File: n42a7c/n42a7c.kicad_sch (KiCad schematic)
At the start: 111 parts, among them J1 Conn_01x02_Pin, J2 Conn_01x02_Pin, SW1 CPG151101S11-16, SW10 CPG151101S11-16, SW11 CPG151101S11-16, SW12 CPG151101S11-16, SW13 CPG151101S11-16, SW14 CPG151101S11-16, SW15 CPG151101S11-16, SW16 CPG151101S11-16, SW17 CPG151101S11-16, SW18 CPG151101S11-16, SW19 CPG151101S11-16, SW2 CPG151101S11-16, SW20 CPG151101S11-16, SW21 CPG151101S11-16, SW22 CPG151101S11-16, SW23 CPG151101S11-16, SW24 CPG151101S11-16, SW25 CPG151101S11-16, SW26 CPG151101S11-16, SW27 CPG151101S11-16, SW28 CPG151101S11-16, SW29 CPG151101S11-16, SW3 CPG151101S11-16, SW30 CPG151101S11-16, SW31 CPG151101S11-16, SW32 CPG151101S11-16, SW33 CPG151101S11-16, SW34 CPG151101S11-16, SW35 CPG151101S11-16, SW36 CPG151101S11-16, SW37 CPG151101S11-16, SW38 CPG151101S11-16, SW39 CPG151101S11-16, SW4 CPG151101S11-16, SW40 CPG151101S11-16, SW41 CPG151101S11-16, SW42 CPG151101S11-16, SW5 CPG151101S11-16, SW6 CPG151101S11-16, SW7 CPG151101S11-16, SW8 CPG151101S11-16, SW9 CPG151101S11-16, U1 XIAO-nRF52840-SMD

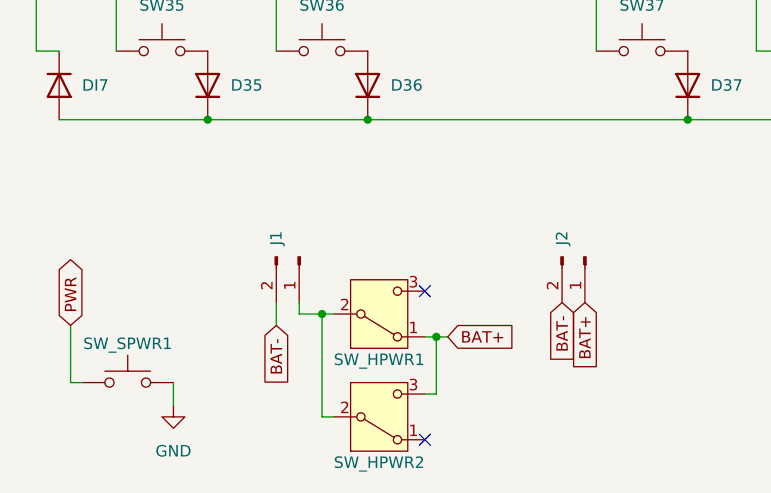
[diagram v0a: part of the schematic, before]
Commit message: revise SSAJ1x0100 footprint / symbol
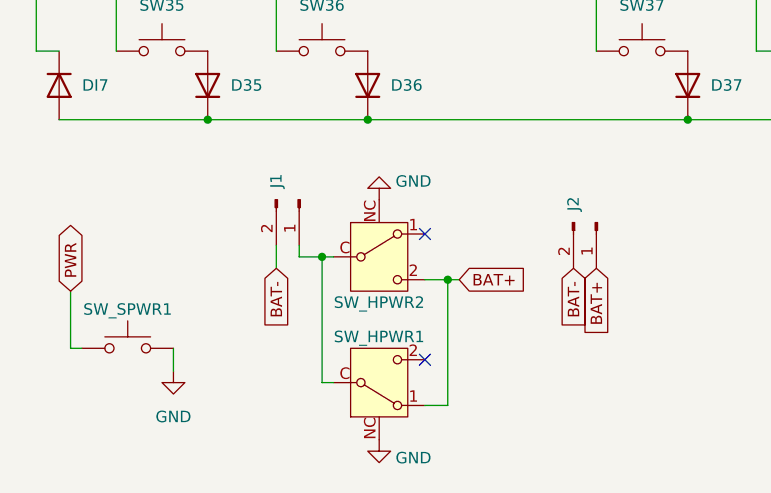
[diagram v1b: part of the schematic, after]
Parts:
- removed SW_HPWR1, SW_HPWR2: SSAJ120100, cscslib:SSAJ120100, symbol Switch:SW_SPDT
- added SW_HPWR1, SW_HPWR2: SSAJ110100, cscslib:SSAJ110100, symbol cscslib:SSAJ1x0100
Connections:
- net BAT+: now also SW_HPWR1.1 (A), SW_HPWR2.2 (C)
- net GND: now also SW_HPWR1.NC, SW_HPWR2.NC
- net at J1.1 (Pin_1): now also SW_HPWR1.C (B), SW_HPWR2.C (B)
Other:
- moved on the sheet: J1, J2, SW_SPWR1

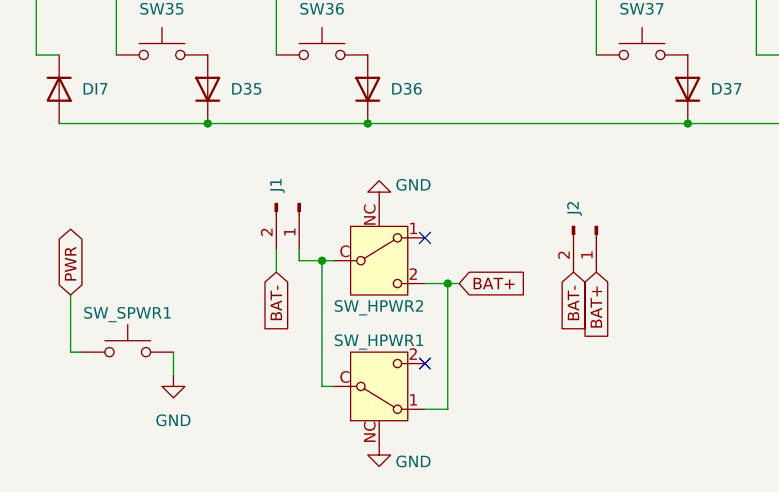
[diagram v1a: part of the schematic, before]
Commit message: revise power connector
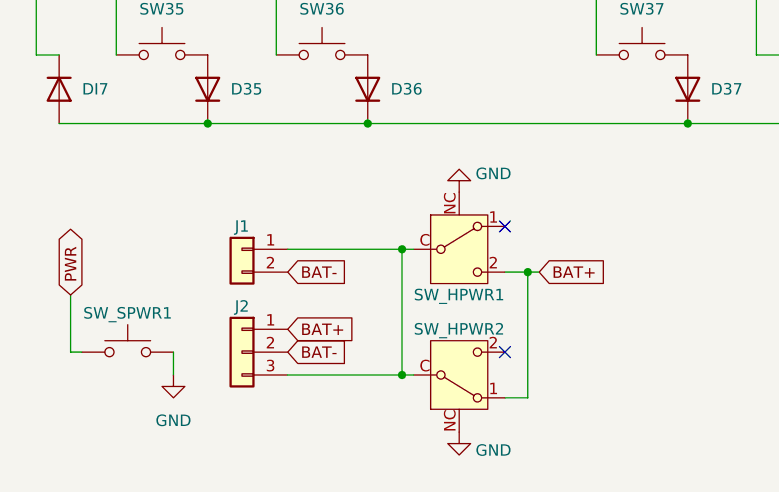
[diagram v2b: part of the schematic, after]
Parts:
- removed J1: Conn_01x02_Pin, Connector_JST:JST_PH_S2B-PH-K_1x02_P2.00mm_Horizontal, symbol Connector:Conn_01x02_Pin
- removed J2: Conn_01x02_Pin, Connector_PinHeader_2.54mm:PinHeader_1x02_P2.54mm_Vertical, symbol Connector:Conn_01x02_Pin
- added J1: Conn_01x02, Connector_JST:JST_PH_S2B-PH-K_1x02_P2.00mm_Horizontal, symbol Connector_Generic:Conn_01x02
- added J2: Conn_01x03, Connector_PinHeader_2.00mm:PinHeader_1x03_P2.00mm_Vertical, symbol Connector_Generic:Conn_01x03
- renumbered SW_HPWR2 to SW_HPWR1, SW_HPWR1 to SW_HPWR2
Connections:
- net BAT+: now also J2.1 (Pin_1)
- net BAT-: now also J1.2 (Pin_2), J2.2 (Pin_2)
- net GND: now also SW_SPWR1.1; no longer SW_SPWR1.2
- net PWR: now also SW_SPWR1.2; no longer SW_SPWR1.1
- net at SW_HPWR1.C (B), SW_HPWR2.C (B): now also J1.1 (Pin_1), J2.3 (Pin_3)
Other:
- moved on the sheet: SW_HPWR1, SW_HPWR2

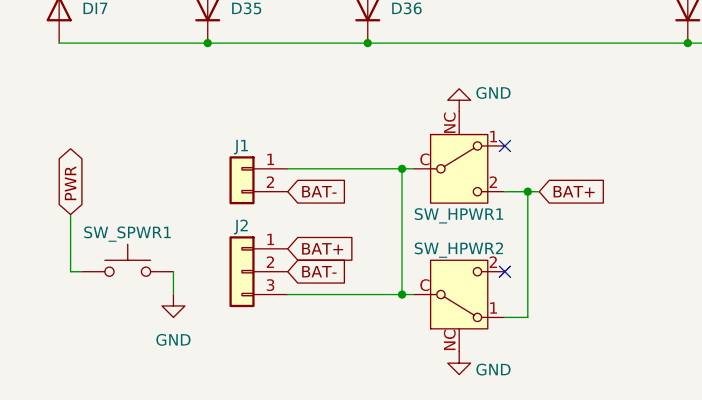
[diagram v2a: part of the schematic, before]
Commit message: revise power SW
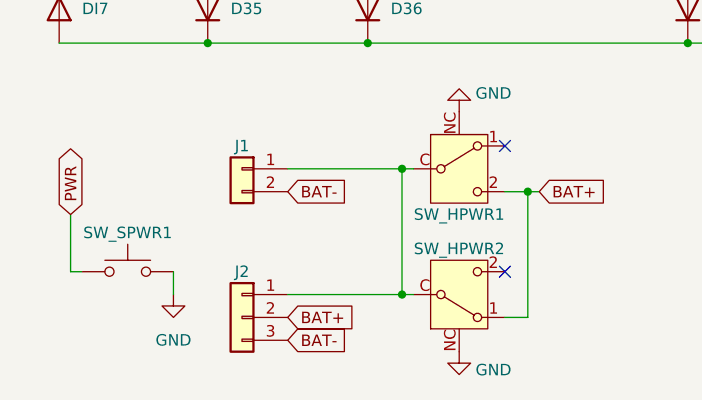
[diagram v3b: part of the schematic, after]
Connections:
- net BAT+: now also J2.2 (Pin_2); no longer J2.1 (Pin_1)
- net BAT-: now also J2.3 (Pin_3); no longer J2.2 (Pin_2)
- net at J1.1 (Pin_1), SW_HPWR1.C (B), SW_HPWR2.C (B): now also J2.1 (Pin_1); no longer J2.3 (Pin_3)
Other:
- moved on the sheet: J2
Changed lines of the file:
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@@
 	(global_label "BAT-"
 		(shape input)
-		(at 43.18 181.61 0)
+		(at 43.18 189.23 0)
 		(effects
 			(font
@@
 		)
 		(property "Intersheetrefs" "${INTERSHEET_REFS}"
-			(at 43.18 181.61 90)
+			(at 43.18 189.23 90)
 			(effects
 				(font
@@
 	(global_label "BAT+"
 		(shape input)
-		(at 43.18 179.07 0)
+		(at 43.18 186.69 0)
 		(effects
 			(font
@@
 		)
 		(property "Intersheetrefs" "${INTERSHEET_REFS}"
-			(at 43.18 179.07 90)
+			(at 43.18 186.69 90)
 			(effects
 				(font
@@
 	(symbol
 		(lib_id "Connector_Generic:Conn_01x03")
-		(at 38.1 181.61 0)
+		(at 38.1 186.69 0)
 		(mirror y)
 		(unit 1)
@@
 		(dnp no)
 		(property "Reference" "J2"
-			(at 38.1 176.53 0)
+			(at 38.1 181.61 0)
 			(effects
 				(font
@@
 		)
 		(property "Value" "Conn_01x03"
-			(at 38.1 187.96 0)
+			(at 38.1 193.04 0)
 			(effects
 				(font
@@
 		)
 		(property "Footprint" "Connector_PinHeader_2.00mm:PinHeader_1x03_P2.00mm_Vertical"
-			(at 38.1 181.61 0)
+			(at 38.1 186.69 0)
 			(effects
 				(font
@@
 		)
 		(property "Datasheet" "~"
-			(at 38.1 181.61 0)
+			(at 38.1 186.69 0)
 			(effects
 				(font
@@
 		)
 		(property "Description" "Generic connector, single row, 01x03, script generated (kicad-library-utils/schlib/autogen/connector/)"
-			(at 38.1 181.61 0)
+			(at 38.1 186.69 0)
 			(effects
 				(font

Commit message: revise switch
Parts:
- J2: footprint Connector_PinHeader_2.00mm:PinHeader_1x03_P2.00mm_Vertical -> Connector_PinHeader_2.00mm:PinHeader_1x04_P2.00mm_Vertical; symbol Connector_Generic:Conn_01x03 -> Connector_Generic:Conn_01x04
- SW_HPWR1: value SSAJ110100 -> SK-12D11; footprint cscslib:SSAJ110100 -> cscslib:SK-12D11
- SW_HPWR2: footprint cscslib:SSAJ110100 -> cscslib:SK-12D11; now not fitted; now left out of the parts list
- SW_SPWR1: value SW_SPWR -> THAU13-AB-R
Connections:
- net BAT+: now also J2.3 (Pin_3); no longer J2.2 (Pin_2)
- net BAT-: now also J2.2 (Pin_2), J2.4 (Pin_4); no longer J2.3 (Pin_3)
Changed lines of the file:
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@@
 	(global_label "BAT-"
 		(shape input)
-		(at 43.18 189.23 0)
+		(at 43.18 191.77 0)
 		(effects
 			(font
@@
 		)
 		(property "Intersheetrefs" "${INTERSHEET_REFS}"
-			(at 43.18 189.23 90)
+			(at 43.18 191.77 90)
 			(effects
 				(font
@@
 		)
 	)
+	(global_label "BAT-"
+		(shape input)
+		(at 43.18 186.69 0)
+		(effects
+			(font
+				(size 1.27 1.27)
+			)
+			(justify left)
+		)
+		(property "Intersheetrefs" "${INTERSHEET_REFS}"
+			(at 43.18 186.69 90)
+			(effects
+				(font
+					(size 1.27 1.27)
+				)
+				(hide yes)
+			)
+		)
+	)
 	(global_label "IO 3"
 		(shape bidirectional)
@@
 	(global_label "BAT+"
 		(shape input)
-		(at 43.18 186.69 0)
+		(at 43.18 189.23 0)
 		(effects
 			(font
@@
 		)
 		(property "Intersheetrefs" "${INTERSHEET_REFS}"
-			(at 43.18 186.69 90)
+			(at 43.18 189.23 90)
 			(effects
 				(font
@@
 			)
 		)
-		(property "Value" "SW_SPWR"
+		(property "Value" "THAU13-AB-R"
 			(at 25.4 183.134 0)
 			(effects
@@
 	)
 	(symbol
-		(lib_id "Connector_Generic:Conn_01x03")
+		(lib_id "Connector_Generic:Conn_01x04")
 		(at 38.1 186.69 0)
 		(mirror y)
@@
 			)
 		)
-		(property "Footprint" "Connector_PinHeader_2.00mm:PinHeader_1x03_P2.00mm_Vertical"
+		(property "Footprint" "Connector_PinHeader_2.00mm:PinHeader_1x04_P2.00mm_Vertical"
 			(at 38.1 186.69 0)
 			(effects
@@
 			)
 		)
-		(property "Description" "Generic connector, single row, 01x03, script generated (kicad-library-utils/schlib/autogen/connector/)"
+		(property "Description" "Generic connector, single row, 01x04, script generated (kicad-library-utils/schlib/autogen/connector/)"
 			(at 38.1 186.69 0)
 			(effects
@@
 		(pin "3"
 		)
+		(pin "4"
+		)
 		(instances
 			(project ""
@@
 		(unit 1)
 		(exclude_from_sim no)
-		(in_bom yes)
-		(on_board yes)
-		(dnp no)
+		(in_bom no)
+		(on_board no)
+		(dnp yes)
 		(property "Reference" "SW_HPWR2"
 			(at 62.23 179.07 0)
@@
 			)
 		)
-		(property "Footprint" "cscslib:SSAJ110100"
+		(property "Footprint" "cscslib:SK-12D11"
 			(at 62.23 184.15 0)
 			(effects
@@
 			)
 		)
-		(property "Value" "SSAJ110100"
+		(property "Value" "SK-12D11"
 			(at 62.23 175.26 0)
 			(effects
@@
 			)
 		)
-		(property "Footprint" "cscslib:SSAJ110100"
+		(property "Footprint" "cscslib:SK-12D11"
 			(at 62.23 170.18 0)
 			(effects

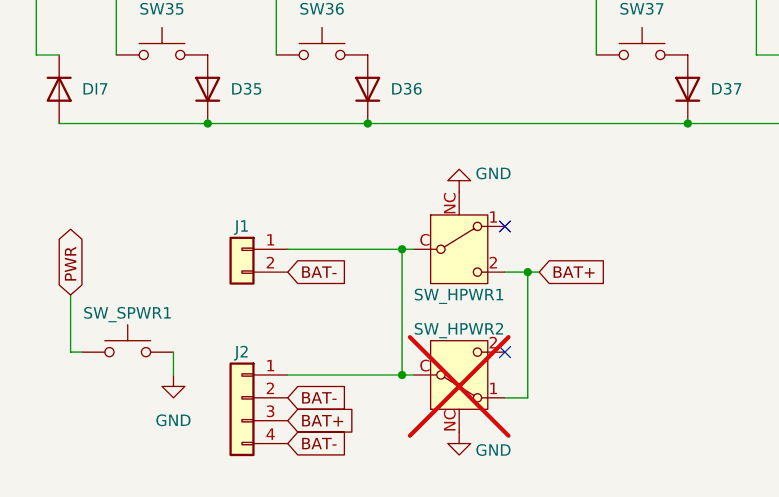
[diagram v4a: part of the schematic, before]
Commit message: revise switch symbol/footprint
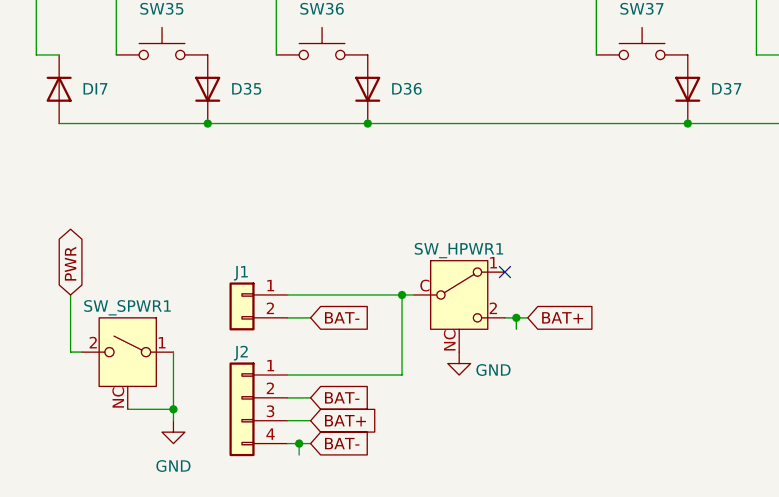
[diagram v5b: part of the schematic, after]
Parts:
- removed SW_HPWR2: SSAJ110100, cscslib:SK-12D11, symbol cscslib:SSAJ1x0100
- SW_HPWR1: symbol cscslib:SSAJ1x0100 -> cscslib:SPDT-NC
- SW_SPWR1: value THAU13-AB-R -> THBP07-043C; symbol cscslib:CPG151101S11 -> cscslib:SPST-NC
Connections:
- net GND: now also SW_SPWR1.NC
- no-connect marks 8 -> 7
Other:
- moved on the sheet: J1, SW_HPWR1

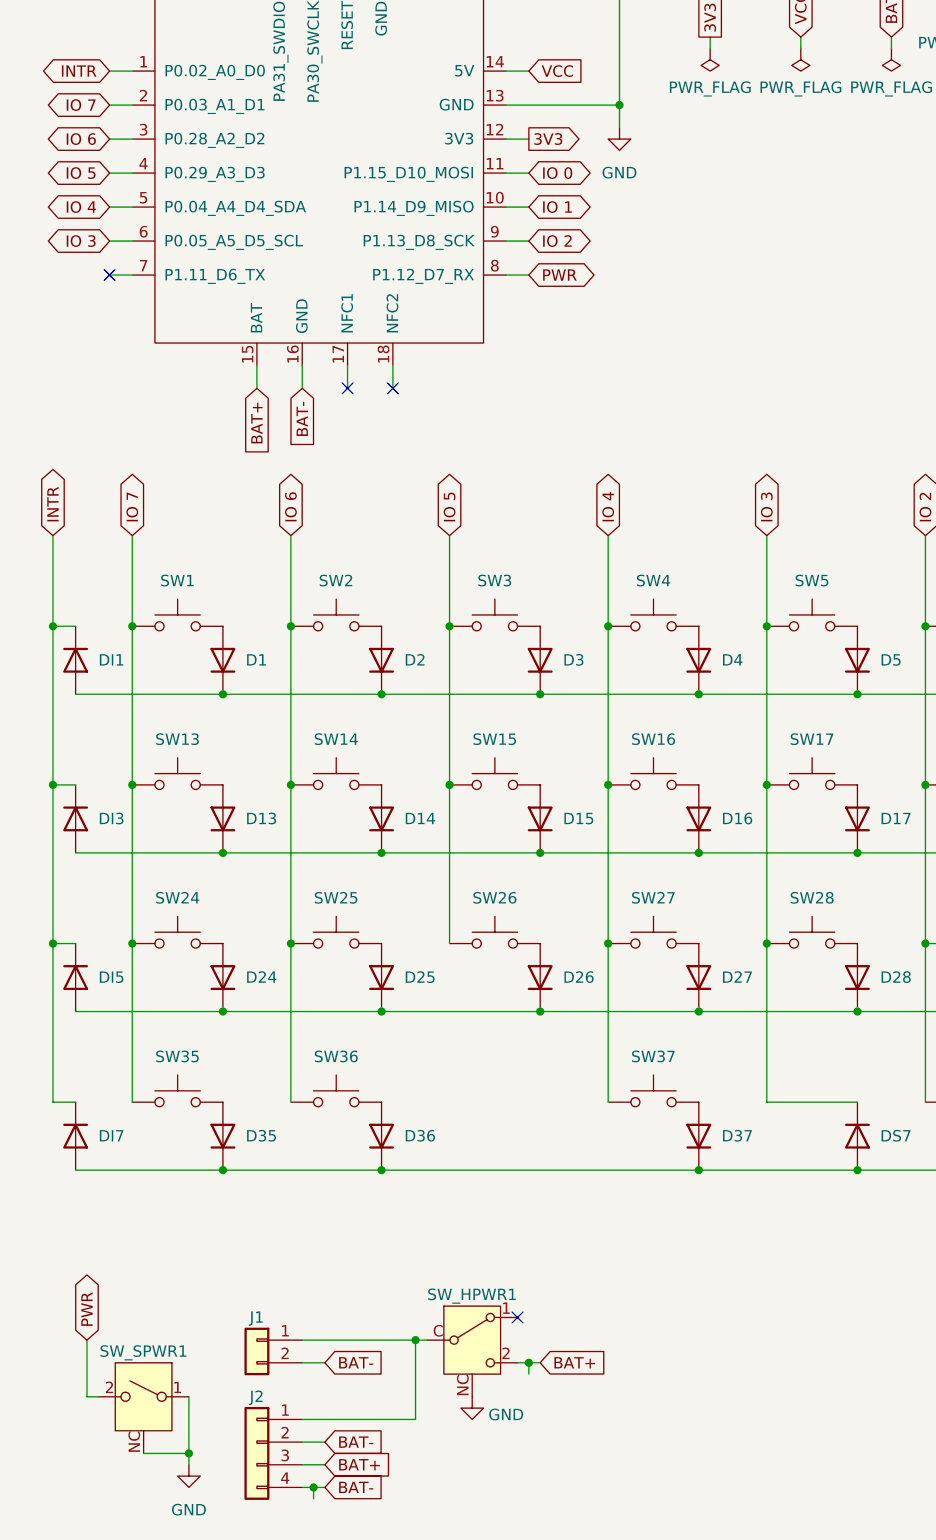
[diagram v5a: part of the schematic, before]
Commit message: create plate
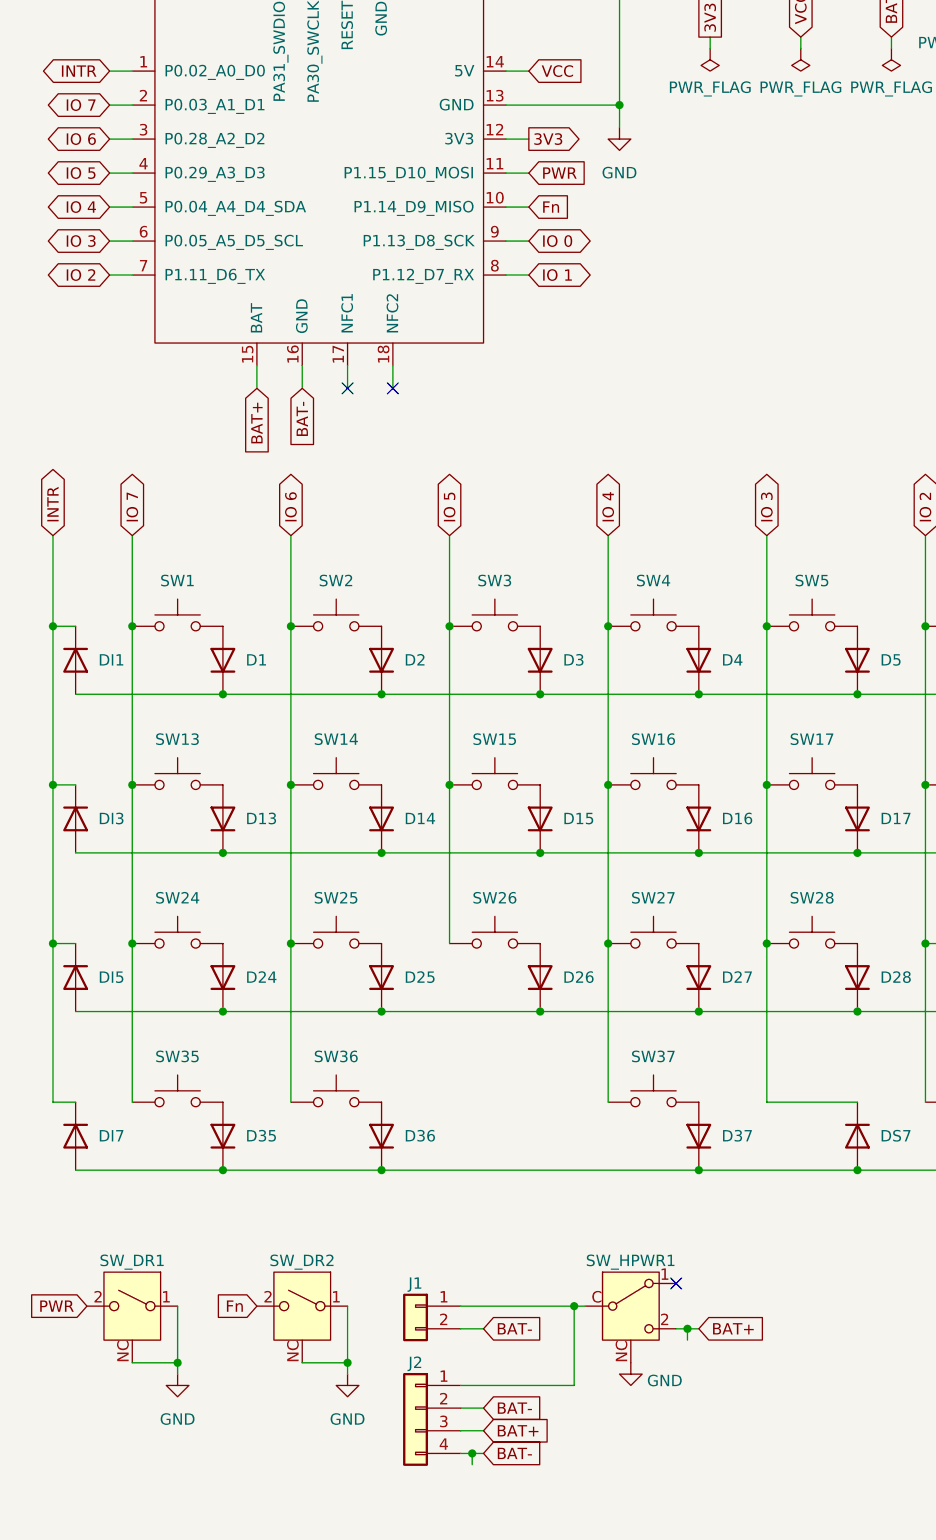
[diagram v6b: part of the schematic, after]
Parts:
- added SW_DR2: SKTDLDE010, cscslib:SKTDLDE010, symbol cscslib:SPST-NC
- SW_DR1: renamed from SW_SPWR1; value THBP07-043C -> SKTDLDE010; footprint cscslib:THBP07-043C -> cscslib:SKTDLDE010
- SW_HPWR1: value SK-12D11 -> SSSS811101; footprint cscslib:SK-12D11 -> cscslib:SSSS811101
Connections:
- net GND: now also SW_DR2.1 (A), SW_DR2.NC
- net IO 0: now also U1.9 (P1.13_D8_SCK); no longer U1.11 (P1.15_D10_MOSI)
- net IO 1: now also U1.8 (P1.12_D7_RX); no longer U1.10 (P1.14_D9_MISO)
- net IO 2: now also U1.7 (P1.11_D6_TX); no longer U1.9 (P1.13_D8_SCK)
- net PWR: now also U1.11 (P1.15_D10_MOSI); no longer U1.8 (P1.12_D7_RX)
- new net Fn: SW_DR2.2 (B), U1.10 (P1.14_D9_MISO)
- no-connect marks 7 -> 6
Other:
- moved on the sheet: J1, J2, SW_DR1, SW_HPWR1

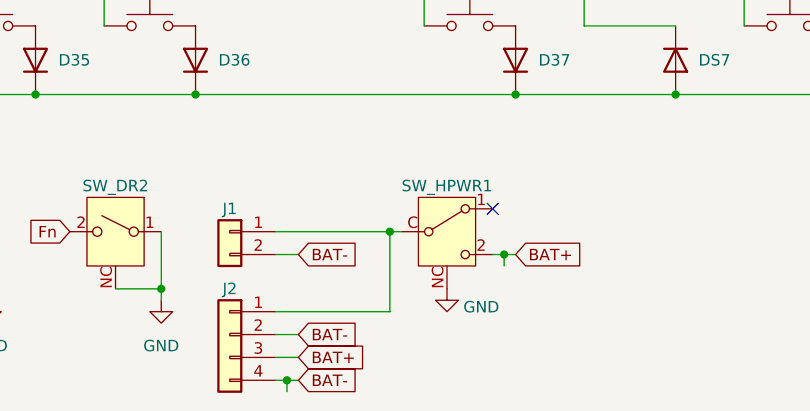
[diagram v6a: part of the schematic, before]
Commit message: revise power line
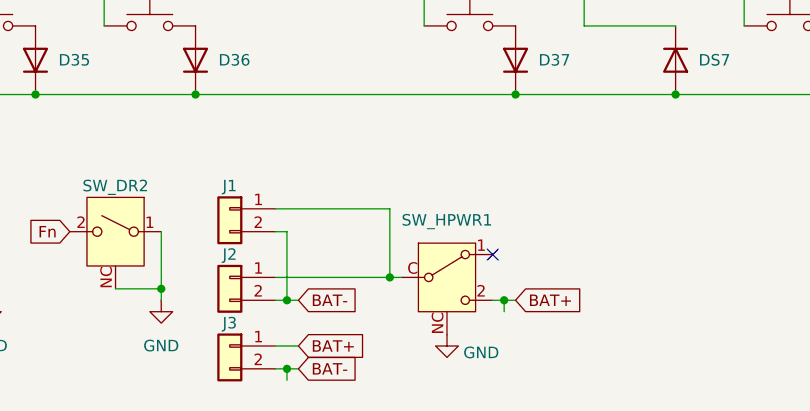
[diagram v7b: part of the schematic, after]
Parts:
- removed J2: Conn_01x03, Connector_PinHeader_2.00mm:PinHeader_1x04_P2.00mm_Vertical, symbol Connector_Generic:Conn_01x04
- added J2, J3: (no value), Connector_PinHeader_2.00mm:PinHeader_1x02_P2.00mm_Vertical, symbol Connector_Generic:Conn_01x02
- J1: value Conn_01x02 -> S2B-PH-SM4-TB; footprint Connector_JST:JST_PH_S2B-PH-K_1x02_P2.00mm_Horizontal -> Connector_JST:JST_PH_S2B-PH-SM4-TB_1x02-1MP_P2.00mm_Horizontal
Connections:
- net BAT+: now also J3.1 (Pin_1)
- net BAT-: now also J2.2 (Pin_2), J3.2 (Pin_2)
- net at J1.1 (Pin_1), SW_HPWR1.C (B): now also J2.1 (Pin_1)
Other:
- moved on the sheet: J1, SW_HPWR1
